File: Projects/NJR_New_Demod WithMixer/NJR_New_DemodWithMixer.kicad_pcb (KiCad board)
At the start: 2 copper layers, 81.3 x 48.3 mm, 32 parts, among them J1 SMA-J-P-H-ST-EM1, U1 SFECF10M7EA00-R0, U2 NJM2549, U3 NJM2741

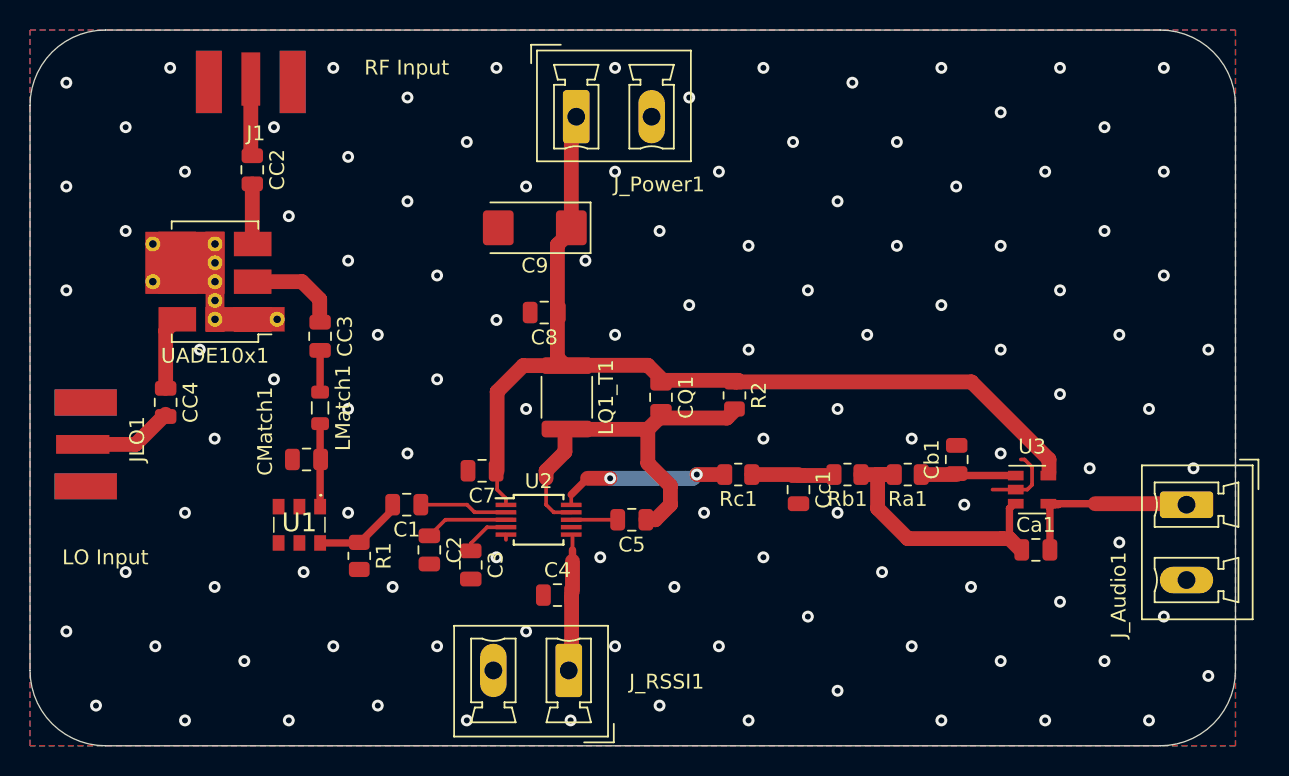
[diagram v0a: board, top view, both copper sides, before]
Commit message: Added a VVA
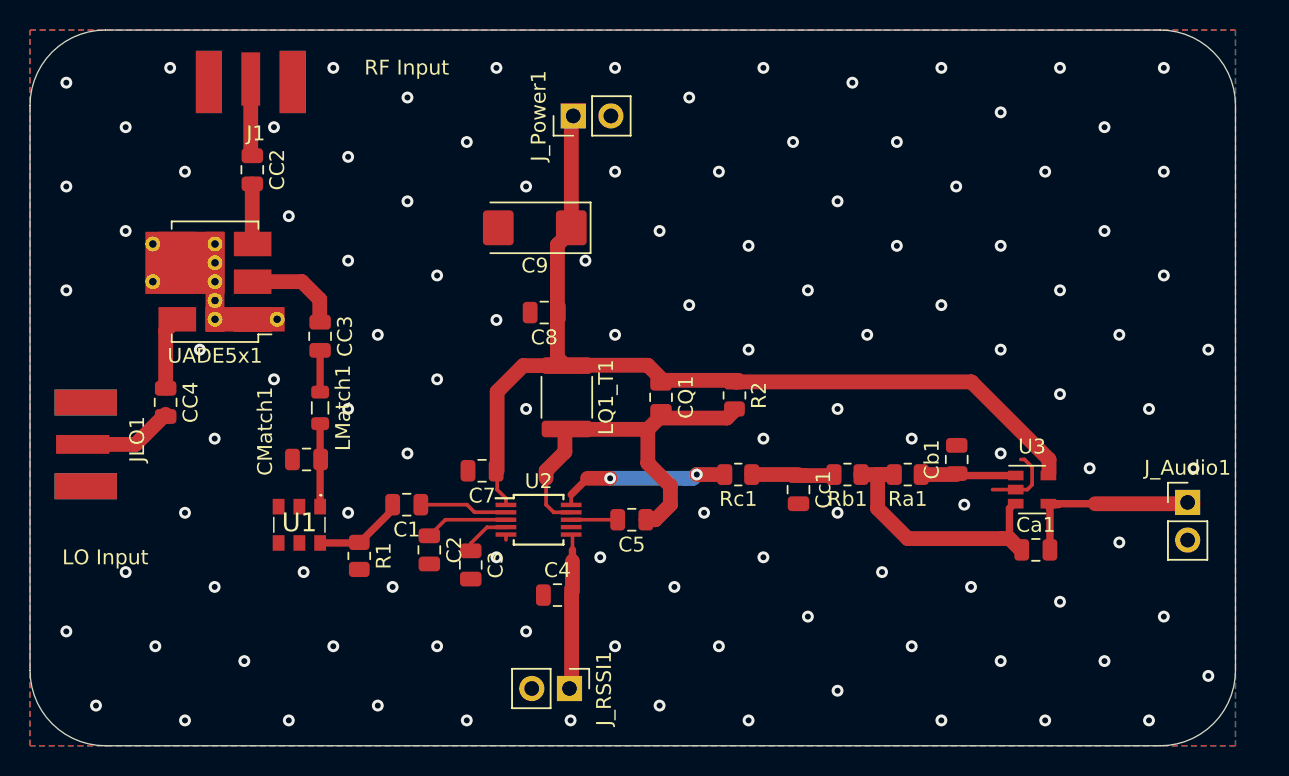
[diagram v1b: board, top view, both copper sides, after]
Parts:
- J_Audio1, J_Power1, J_RSSI1: footprint Connector_Phoenix_MC_HighVoltage:PhoenixContact_MCV_1,5_2-G-5.08_1x02_P5.08mm_Vertical -> Connector_PinHeader_2.54mm:PinHeader_1x02_P2.54mm_Vertical
- moved J_RSSI1 1.22 mm to (115.1, 102.8), turned to 270 degrees
- moved J_Power1 0.21 mm to (115.4, 64.2), turned to 90 degrees
- moved J_Audio1 0.17 mm to (156.8, 90.3), turned to 0 degrees
- renumbered UADE10x1 to UADE5x1
